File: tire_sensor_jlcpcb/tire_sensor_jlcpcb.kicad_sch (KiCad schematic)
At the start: 37 parts, among them J1 Conn_02x05_Odd_Even, U2 DPS368, U3 LSM6DS3, X1 NX2016SA-32MHZ-EXS00A-CS06654, X2 32.768kHz

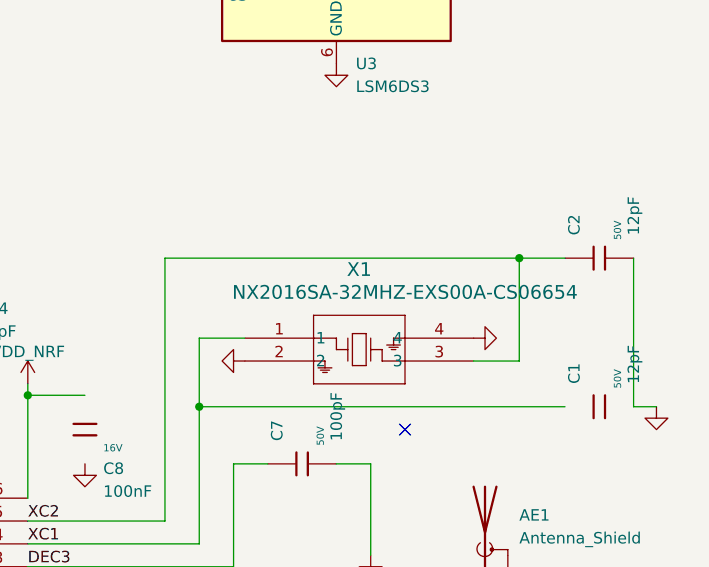
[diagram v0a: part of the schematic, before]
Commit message: Swap crystal to FA-128 and regen fab outputs
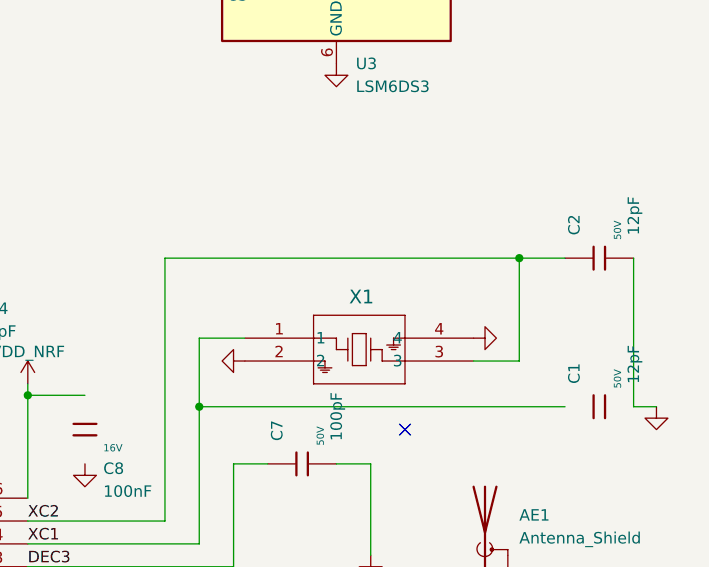
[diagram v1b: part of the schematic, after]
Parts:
- X1: footprint NX2016SA_NDK -> FA-128_EPS; symbol NX2016SA_NDK:NX2016SA-32MHZ-EXS00A-CS06654 -> FA_128_EPS:FA-128_32.0000MF10Z-AJ3
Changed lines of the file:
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@@
 	)
 	(symbol
-		(lib_id "NX2016SA_NDK:NX2016SA-32MHZ-EXS00A-CS06654")
+		(lib_id "FA_128_EPS:FA-128_32.0000MF10Z-AJ3")
 		(at 208.28 91.44 0)
 		(unit 1)
@@
 		(dnp no)
 		(property "Reference" "X1"
-			(at 220.98 83.82 0)
+			(at 221.234 86.868 0)
 			(effects
 				(font
@@
 					(size 1.524 1.524)
 				)
+				(hide yes)
 			)
 		)
-		(property "Footprint" "NX2016SA_NDK"
+		(property "Footprint" "FA-128_EPS"
 			(at 208.28 91.44 0)
 			(effects
@@
 			)
 		)
-		(property "Datasheet" "NX2016SA-32MHZ-EXS00A-CS06654"
+		(property "Datasheet" "FA-128 32.0000MF10Z-AJ3"
 			(at 208.28 91.44 0)
 			(effects
